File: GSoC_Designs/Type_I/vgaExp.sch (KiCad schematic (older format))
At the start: 52 parts, among them J1 DE-15, J2 DE-15, J3 VHDCI, P1 50R, P2 50R, P3 50R, P4 50R, P5 CONN_1, P6 CONN_1, U3 AD9984

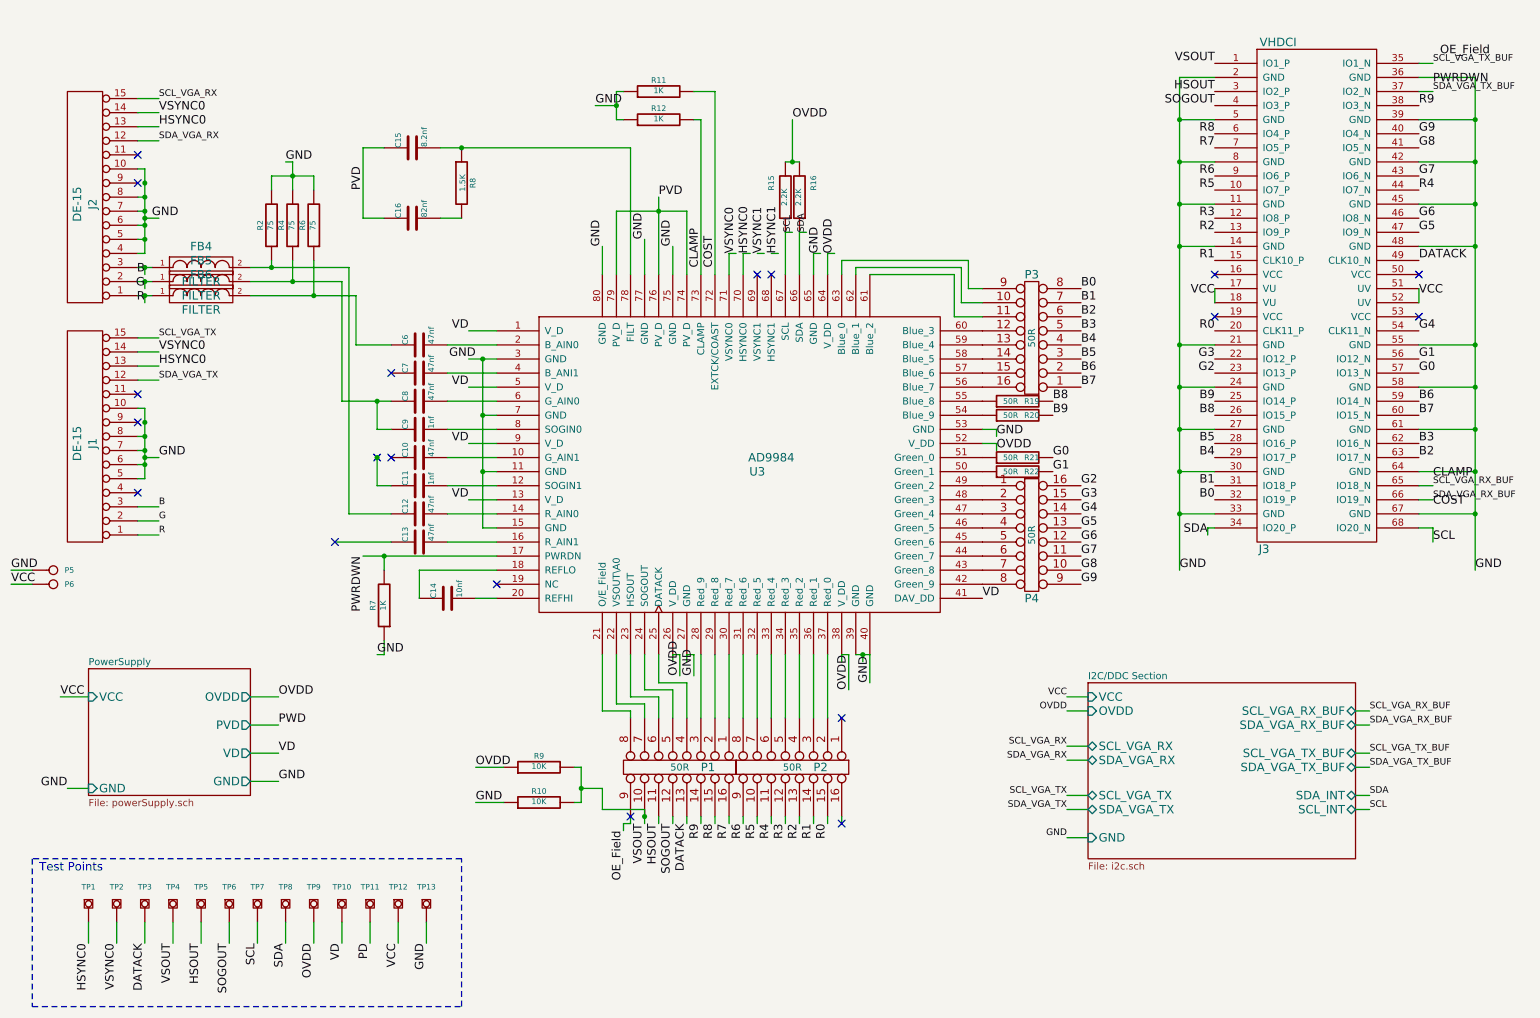
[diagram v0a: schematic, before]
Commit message: Added header for unused Pins
Unused pins are OE_Field, COAST, CLAMP and PWRDWN
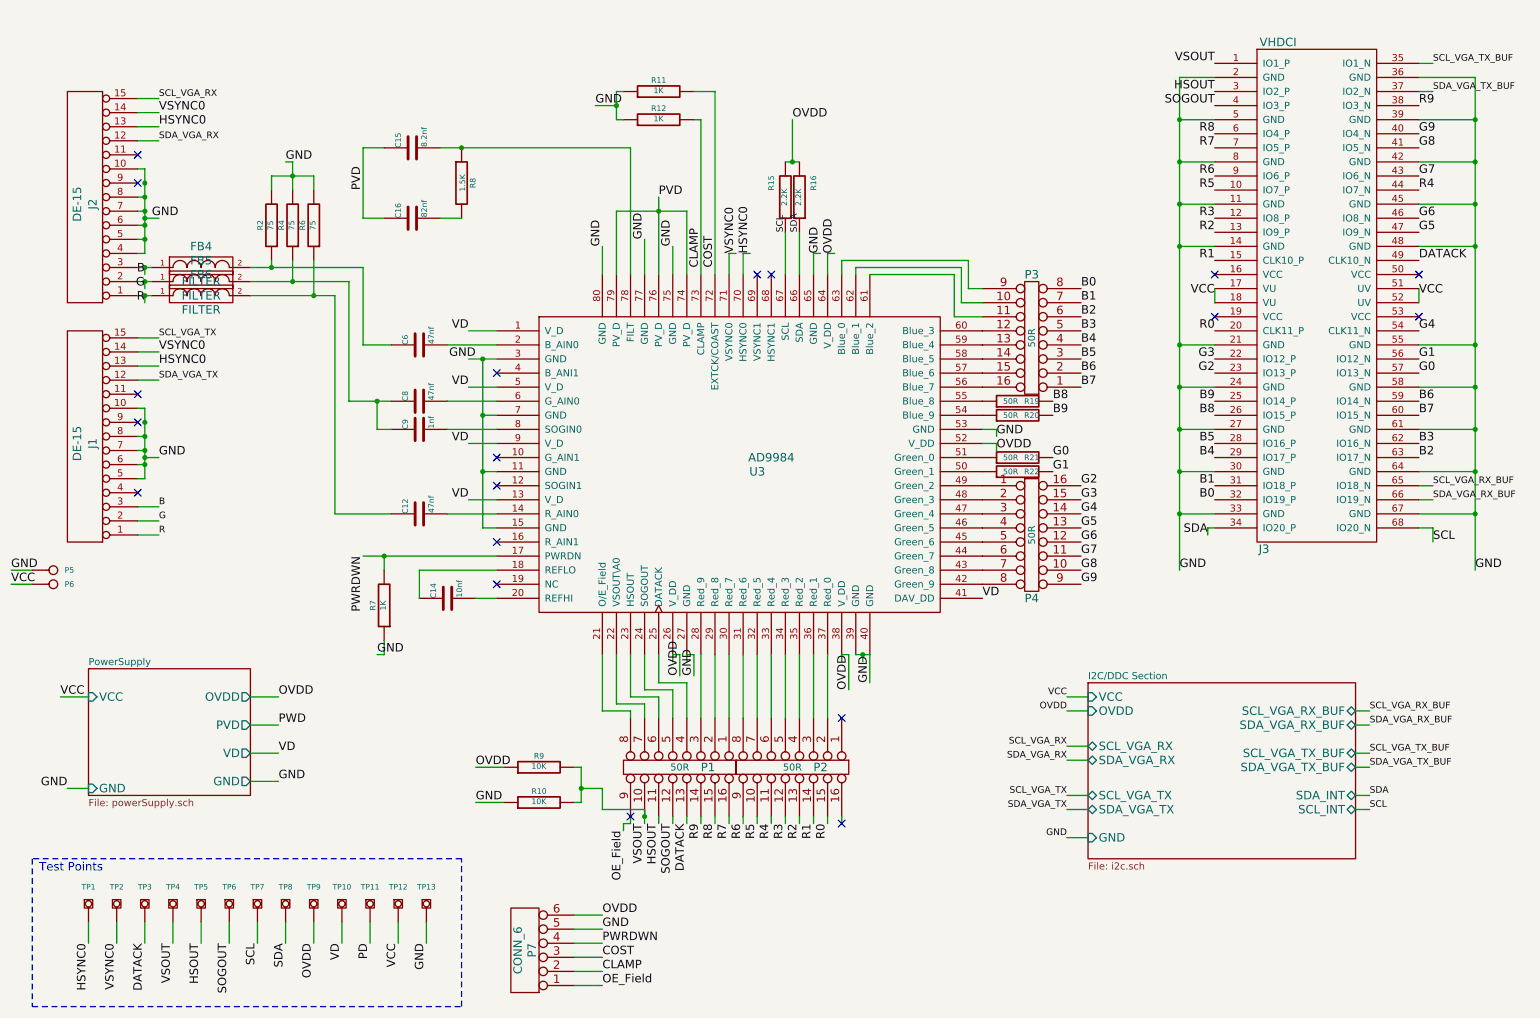
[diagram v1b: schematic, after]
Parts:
- removed C10, C13, C7: 47nf, ~, symbol C
- removed C11: 1nf, ~, symbol C
- added P7: CONN_6, symbol CONN_6
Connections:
- net CLAMP: now also P7.2
- net COST: now also P7.3
- net GND: now also P7.5
- net OE_Field: now also P7.1
- net OVDD: now also P7.6
- net PWRDWN: now also P7.4
- net at FB6.2, R6.1: now also C12.1; no longer C6.1
- net at FB4.2, R2.1: now also C6.1; no longer C12.1

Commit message: PCB Routing
70% tracks routed. Fine tuning remaining
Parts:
- removed P1, P2, P3, P4: 50R, symbol DIL16
- removed R19, R20, R21, R22: 50R, ~, symbol R
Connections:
- net PD is gone; now on net PVD: TP11.1
- net B0: now also U3.63 (Blue_0)
- net B1: now also U3.62 (Blue_1)
- net B2: now also U3.61 (Blue_2)
- net B3: now also U3.60 (Blue_3)
- net B4: now also U3.59 (Blue_4)
- net B5: now also U3.58 (Blue_5)
- net B6: now also U3.57 (Blue_6)
- net B7: now also U3.56 (Blue_7)
- net B8: now also U3.55 (Blue_8)
- net B9: now also U3.54 (Blue_9)
- net DATACK: now also U3.25 (DATACK)
- net G0: now also U3.51 (Green_0)
- net G1: now also U3.50 (Green_1)
- net G2: now also U3.49 (Green_2)
- net G3: now also U3.48 (Green_3)
- net G4: now also U3.47 (Green_4)
- net G5: now also U3.46 (Green_5)
- net G6: now also U3.45 (Green_6)
- net G7: now also U3.44 (Green_7)
- net G8: now also U3.43 (Green_8)
- net G9: now also U3.42 (Green_9)
- net GND: now also U3.68 (HSYNC1), U3.69 (VSYNC1); no longer J2.4 (P4)
- net HSOUT: now also U3.23 (HSOUT)
- net OE_Field: now also U3.21 (O/E_Field)
- net R0: now also U3.37 (Red_0)
- net R1: now also U3.36 (Red_1)
- net R2: now also U3.35 (Red_2)
- net R3: now also U3.34 (Red_3)
- net R4: now also U3.33 (Red_4)
- net R5: now also U3.32 (Red_5)
- net R6: now also U3.31 (Red_6)
- net R7: now also U3.30 (Red_7)
- net R8: now also U3.29 (Red_8)
- net R9: now also U3.28 (Red_9)
- net SCL_VGA_RX_BUF: now also J3.35 (IO1_N); no longer J3.65 (IO18_N)
- net SCL_VGA_TX_BUF: now also J3.65 (IO18_N); no longer J3.35 (IO1_N)
- net SDA_VGA_RX_BUF: now also J3.37 (IO2_N); no longer J3.66 (IO19_N)
- net SDA_VGA_TX_BUF: now also J3.66 (IO19_N); no longer J3.37 (IO2_N)
- net SOGOUT: now also U3.24 (SOGOUT)
- net VSOUT: now also U3.22 (VSOUT\A0)
- net at C15.2, U3.78 (FILT): now also R8.2; no longer R8.1
- net at C16.2: now also R8.1; no longer R8.2
- net at FB4.2, R2.1: now also C12.1; no longer C6.1
- net at FB6.2, R6.1: now also C6.1; no longer C12.1
- no-connect marks 19 -> 15
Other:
- moved on the sheet: C12, C14, C15, C16, C6, C8, C9, FB4, FB5, FB6, J1, J2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
